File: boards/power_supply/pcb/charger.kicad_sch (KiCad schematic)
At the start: 42 parts, among them J301 Conn_01x02_Socket, J302 Conn_01x04_Socket

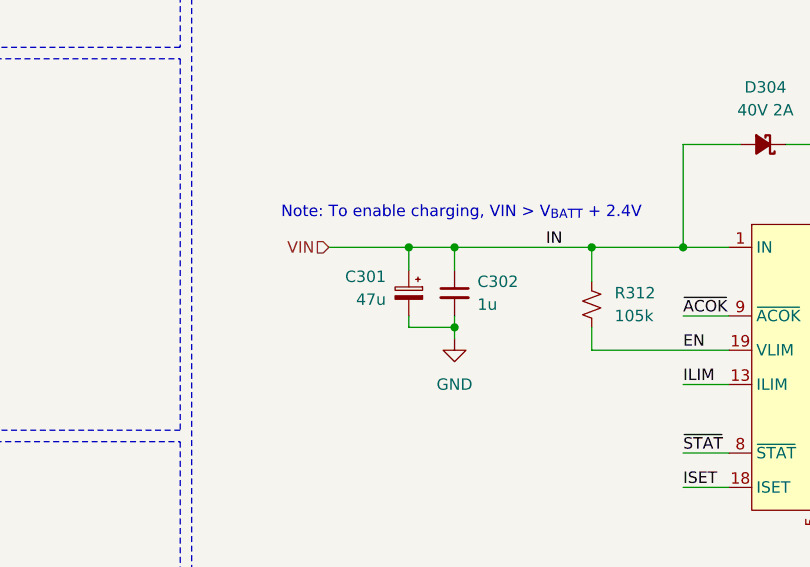
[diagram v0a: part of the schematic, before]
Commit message: psu schematic capture
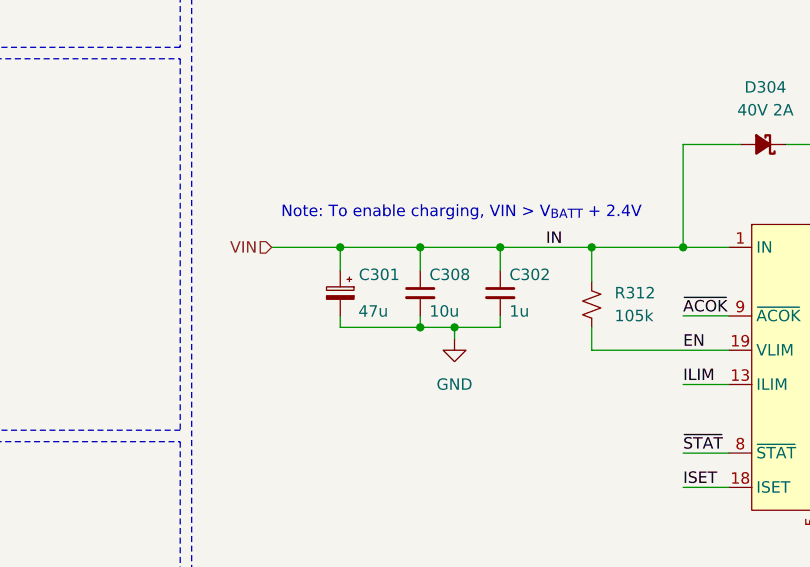
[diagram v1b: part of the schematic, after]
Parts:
- added C308: 10u, symbol Device:C_Small
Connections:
- net GND: now also C308.2
- net VIN: now also C308.1
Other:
- moved on the sheet: C301
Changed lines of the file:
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@@
 	)
 	(junction
-		(at 146.05 80.01)
+		(at 147.32 88.9)
 		(diameter 0)
 		(color 0 0 0 0)
@@
 	)
 	(junction
+		(at 147.32 80.01)
+		(diameter 0)
+		(color 0 0 0 0)
+	)
+	(junction
 		(at 240.03 99.06)
 		(diameter 0)
@@
 	)
 	(junction
-		(at 151.13 80.01)
+		(at 138.43 80.01)
 		(diameter 0)
 		(color 0 0 0 0)
@@
 	)
 	(junction
+		(at 156.21 80.01)
+		(diameter 0)
+		(color 0 0 0 0)
+	)
+	(junction
 		(at 198.12 113.03)
 		(diameter 0)
@@
 	(wire
 		(pts
-			(xy 151.13 80.01) (xy 151.13 82.55)
+			(xy 156.21 80.01) (xy 156.21 82.55)
 		)
 		(stroke
@@
 	(wire
 		(pts
-			(xy 146.05 80.01) (xy 151.13 80.01)
+			(xy 64.77 72.39) (xy 64.77 73.66)
 		)
 		(stroke
@@
 	(wire
 		(pts
-			(xy 64.77 72.39) (xy 64.77 73.66)
+			(xy 176.53 80.01) (xy 181.61 80.01)
 		)
 		(stroke
@@
 	(wire
 		(pts
-			(xy 176.53 80.01) (xy 181.61 80.01)
+			(xy 151.13 88.9) (xy 151.13 90.17)
 		)
 		(stroke
@@
 	(wire
 		(pts
-			(xy 151.13 88.9) (xy 151.13 90.17)
+			(xy 138.43 80.01) (xy 147.32 80.01)
 		)
 		(stroke
@@
 	(wire
 		(pts
-			(xy 151.13 80.01) (xy 166.37 80.01)
-		)
-		(stroke
-			(width 0)
-			(type default)
-		)
-	)
-	(wire
-		(pts
 			(xy 39.37 44.45) (xy 39.37 45.72)
 		)
@@
 	(wire
 		(pts
-			(xy 146.05 88.9) (xy 151.13 88.9)
+			(xy 138.43 88.9) (xy 147.32 88.9)
 		)
 		(stroke
@@
 	(wire
 		(pts
+			(xy 156.21 80.01) (xy 166.37 80.01)
+		)
+		(stroke
+			(width 0)
+			(type default)
+		)
+	)
+	(wire
+		(pts
 			(xy 64.77 44.45) (xy 64.77 45.72)
 		)
@@
 	(wire
 		(pts
-			(xy 137.16 80.01) (xy 146.05 80.01)
+			(xy 130.81 80.01) (xy 138.43 80.01)
 		)
 		(stroke
@@
 	(wire
 		(pts
+			(xy 147.32 80.01) (xy 147.32 82.55)
+		)
+		(stroke
+			(width 0)
+			(type default)
+		)
+	)
+	(wire
+		(pts
 			(xy 229.87 54.61) (xy 229.87 59.69)
 		)
@@
 	(wire
 		(pts
-			(xy 146.05 87.63) (xy 146.05 88.9)
+			(xy 138.43 87.63) (xy 138.43 88.9)
 		)
 		(stroke
@@
 	(wire
 		(pts
+			(xy 147.32 88.9) (xy 151.13 88.9)
+		)
+		(stroke
+			(width 0)
+			(type default)
+		)
+	)
+	(wire
+		(pts
 			(xy 207.01 76.2) (xy 210.82 76.2)
 		)
@@
 	(wire
 		(pts
-			(xy 146.05 80.01) (xy 146.05 82.55)
+			(xy 138.43 80.01) (xy 138.43 82.55)
+		)
+		(stroke
+			(width 0)
+			(type default)
+		)
+	)
+	(wire
+		(pts
+			(xy 147.32 87.63) (xy 147.32 88.9)
 		)
 		(stroke
@@
 	(wire
 		(pts
+			(xy 147.32 80.01) (xy 156.21 80.01)
+		)
+		(stroke
+			(width 0)
+			(type default)
+		)
+	)
+	(wire
+		(pts
 			(xy 50.8 161.29) (xy 50.8 162.56)
 		)
@@
 	(wire
 		(pts
+			(xy 156.21 88.9) (xy 151.13 88.9)
+		)
+		(stroke
+			(width 0)
+			(type default)
+		)
+	)
+	(wire
+		(pts
 			(xy 194.31 74.93) (xy 194.31 68.58)
 		)
@@
 	(wire
 		(pts
-			(xy 151.13 87.63) (xy 151.13 88.9)
+			(xy 156.21 87.63) (xy 156.21 88.9)
 		)
 		(stroke
@@
 	(hierarchical_label "VIN"
 		(shape input)
-		(at 137.16 80.01 180)
+		(at 130.81 80.01 180)
 		(fields_autoplaced yes)
 		(effects
@@
 	)
 	(symbol
-		(lib_id "Device:C_Small")
-		(at 151.13 85.09 0)
-		(unit 1)
-		(exclude_from_sim no)
-		(in_bom yes)
-		(on_board yes)
-		(dnp no)
-		(fields_autoplaced yes)
-		(property "Reference" "C302"
-			(at 153.67 83.8262 0)
-			(effects
-				(font
-					(size 1.27 1.27)
-				)
-				(justify left)
-			)
-		)
-		(property "Value" "1u"
-			(at 153.67 86.3662 0)
-			(effects
-				(font
-					(size 1.27 1.27)
-				)
-				(justify left)
-			)
-		)
-		(property "Footprint" ""
-			(at 151.13 85.09 0)
-			(effects
-				(font
-					(size 1.27 1.27)
-				)
-				(hide yes)
-			)
-		)
-		(property "Datasheet" "~"
-			(at 151.13 85.09 0)
-			(effects
-				(font
-					(size 1.27 1.27)
-				)
-				(hide yes)
-			)
-		)
-		(property "Description" "Unpolarized capacitor, small symbol"
-			(at 151.13 85.09 0)
-			(effects
-				(font
-					(size 1.27 1.27)
-				)
-				(hide yes)
-			)
-		)
-		(pin "1"
-		)
-		(pin "2"
-		)
-		(instances
-			(project "power_supply"
-				(path "/6a7d9dc9-f78f-470f-911b-b95256023173/00f00675-e615-4796-971e-104476714f1d"
-					(reference "C302")
-					(unit 1)
-				)
-			)
-		)
-	)
-	(symbol
 		(lib_id "power:GND")
 		(at 29.21 177.8 0)
@@
 	(symbol
 		(lib_id "Device:C_Polarized_Small")
-		(at 146.05 85.09 0)
+		(at 138.43 85.09 0)
 		(mirror y)
 		(unit 1)
@@
 		(dnp no)
 		(property "Reference" "C301"
-			(at 143.51 83.2738 0)
+			(at 145.034 83.058 0)
 			(effects
 				(font
@@
 		)
 		(property "Value" "47u"
-			(at 143.51 85.8138 0)
+			(at 143.764 87.122 0)
 			(effects
 				(font
@@
 		)
 		(property "Footprint" ""
-			(at 146.05 85.09 0)
+			(at 138.43 85.09 0)
 			(effects
 				(font
@@
 		)
 		(property "Datasheet" "~"
-			(at 146.05 85.09 0)
+			(at 138.43 85.09 0)
 			(effects
 				(font
@@
 		)
 		(property "Description" "Polarized capacitor, small symbol"
-			(at 146.05 85.09 0)
+			(at 138.43 85.09 0)
 			(effects
 				(font
@@
 	)
 	(symbol
+		(lib_id "Device:C_Small")
+		(at 147.32 85.09 0)
+		(unit 1)
+		(exclude_from_sim no)
+		(in_bom yes)
+		(on_board yes)
+		(dnp no)
+		(property "Reference" "C308"
+			(at 148.336 83.058 0)
+			(effects
+				(font
+					(size 1.27 1.27)
+				)
+				(justify left)
+			)
+		)
+		(property "Value" "10u"
+			(at 148.336 87.122 0)
+			(effects
+				(font
+					(size 1.27 1.27)
+				)
+				(justify left)
+			)
+		)
+		(property "Footprint" ""
+			(at 147.32 85.09 0)
+			(effects
+				(font
+					(size 1.27 1.27)
+				)
+				(hide yes)
+			)
+		)
+		(property "Datasheet" "~"
+			(at 147.32 85.09 0)
+			(effects
+				(font
+					(size 1.27 1.27)
+				)
+				(hide yes)
+			)
+		)
+		(property "Description" "Unpolarized capacitor, small symbol"
+			(at 147.32 85.09 0)
+			(effects
+				(font
+					(size 1.27 1.27)
+				)
+				(hide yes)
+			)
+		)
+		(pin "1"
+		)
+		(pin "2"
+		)
+		(instances
+			(project "power_supply"
+				(path "/6a7d9dc9-f78f-470f-911b-b95256023173/00f00675-e615-4796-971e-104476714f1d"
+					(reference "C308")
+					(unit 1)
+				)
+			)
+		)
+	)
+	(symbol
 		(lib_id "power:GND")
 		(at 39.37 134.62 0)
@@
 					(unit 1)
 				)
+			)
+		)
+	)
+	(symbol
+		(lib_id "Device:C_Small")
+		(at 156.21 85.09 0)
+		(unit 1)
+		(exclude_from_sim no)
+		(in_bom yes)
+		(on_board yes)
+		(dnp no)
+		(property "Reference" "C302"
+			(at 157.226 83.058 0)
+			(effects
+				(font
+					(size 1.27 1.27)
+				)
+				(justify left)
+			)
+		)
+		(property "Value" "1u"
+			(at 157.226 87.122 0)
+			(effects
+				(font
+					(size 1.27 1.27)
+				)
+				(justify left)
+			)
+		)
+		(property "Footprint" ""
+			(at 156.21 85.09 0)
+			(effects
+				(font
+					(size 1.27 1.27)
+				)
+				(hide yes)
+			)
+		)
+		(property "Datasheet" "~"
+			(at 156.21 85.09 0)
+			(effects
+				(font
+					(size 1.27 1.27)
+				)
+				(hide yes)
+			)
+		)
+		(property "Description" "Unpolarized capacitor, small symbol"
+			(at 156.21 85.09 0)
+			(effects
+				(font
+					(size 1.27 1.27)
+				)
+				(hide yes)
+			)
+		)
+		(pin "1"
+		)
+		(pin "2"
+		)
+		(instances
+			(project "power_supply"
+				(path "/6a7d9dc9-f78f-470f-911b-b95256023173/00f00675-e615-4796-971e-104476714f1d"
+					(reference "C302")
+					(unit 1)
+				)

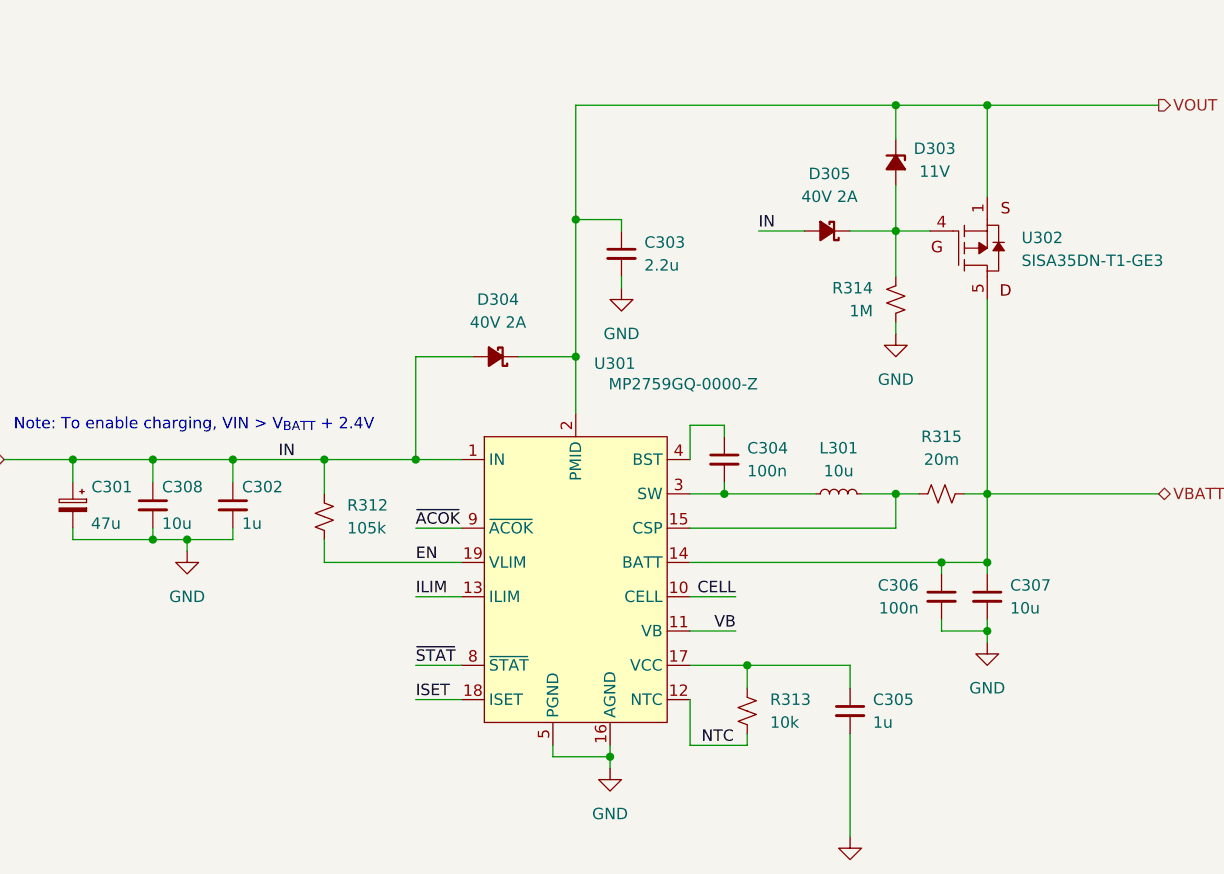
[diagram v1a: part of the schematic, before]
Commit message: psu schematic capture
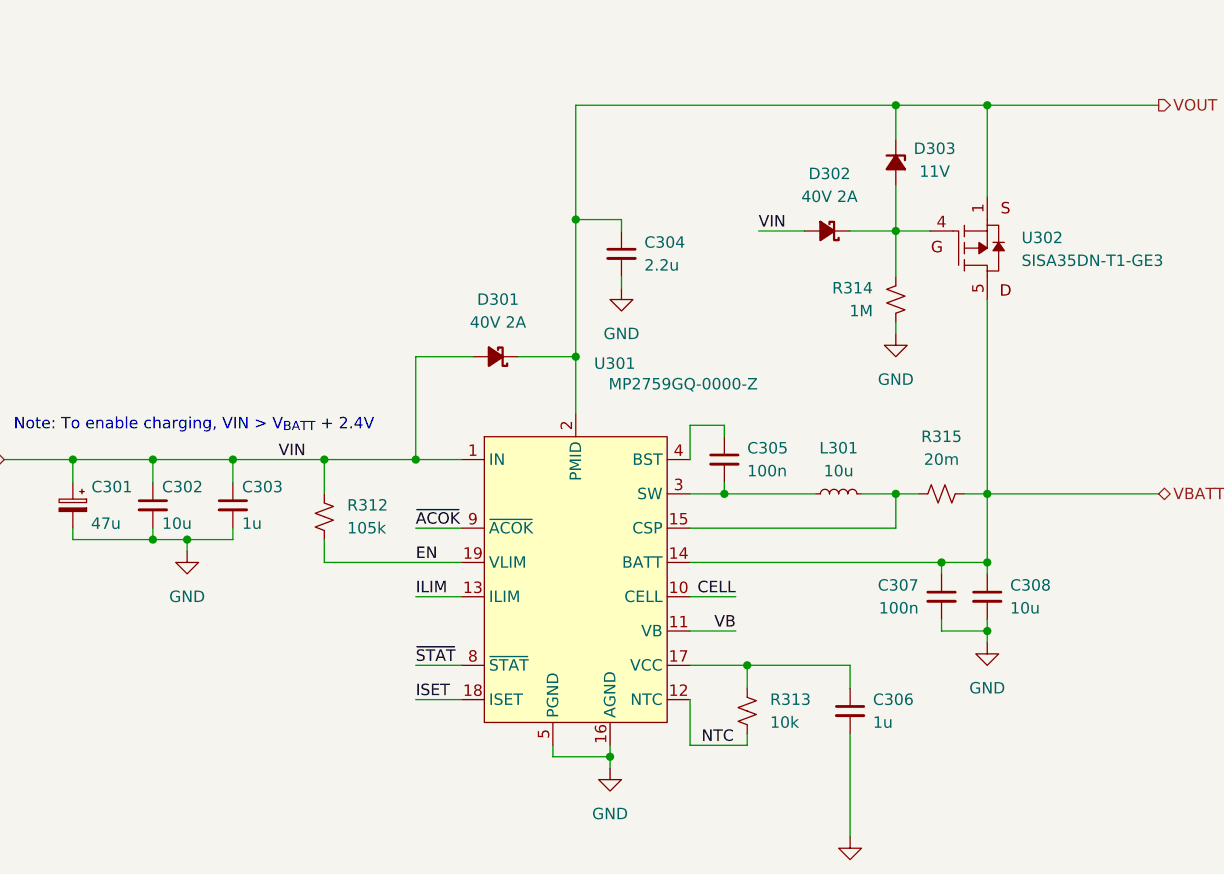
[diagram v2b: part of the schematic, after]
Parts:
- renumbered C308 to C302, C302 to C303, C303 to C304, C304 to C305, C305 to C306, C306 to C307, C307 to C308, D304 to D301, D305 to D302
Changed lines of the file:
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@@
 		)
 	)
-	(label "IN"
+	(label "VIN"
 		(at 161.29 80.01 0)
 		(fields_autoplaced yes)
@@
 		)
 	)
-	(label "IN"
+	(label "VIN"
 		(at 214.63 54.61 0)
 		(fields_autoplaced yes)
@@
 		(dnp no)
 		(fields_autoplaced yes)
-		(property "Reference" "D305"
+		(property "Reference" "D302"
 			(at 222.504 48.26 0)
 			(effects
@@
 			(project "power_supply"
 				(path "/6a7d9dc9-f78f-470f-911b-b95256023173/00f00675-e615-4796-971e-104476714f1d"
-					(reference "D305")
+					(reference "D302")
 					(unit 1)
 				)
@@
 		(on_board yes)
 		(dnp no)
-		(property "Reference" "C306"
+		(property "Reference" "C307"
 			(at 232.41 93.9862 0)
 			(effects
@@
 			(project "power_supply"
 				(path "/6a7d9dc9-f78f-470f-911b-b95256023173/00f00675-e615-4796-971e-104476714f1d"
-					(reference "C306")
+					(reference "C307")
 					(unit 1)
 				)
@@
 		(dnp no)
 		(fields_autoplaced yes)
-		(property "Reference" "C307"
+		(property "Reference" "C308"
 			(at 242.57 93.9862 0)
 			(effects
@@
 			(project "power_supply"
 				(path "/6a7d9dc9-f78f-470f-911b-b95256023173/00f00675-e615-4796-971e-104476714f1d"
-					(reference "C307")
+					(reference "C308")
 					(unit 1)
 				)
@@
 		(dnp no)
 		(fields_autoplaced yes)
-		(property "Reference" "C305"
+		(property "Reference" "C306"
 			(at 227.33 106.6862 0)
 			(effects
@@
 			(project ""
 				(path "/6a7d9dc9-f78f-470f-911b-b95256023173/00f00675-e615-4796-971e-104476714f1d"
-					(reference "C305")
+					(reference "C306")
 					(unit 1)
 				)
@@
 		(on_board yes)
 		(dnp no)
-		(property "Reference" "C308"
+		(property "Reference" "C302"
 			(at 148.336 83.058 0)
 			(effects
@@
 			(project "power_supply"
 				(path "/6a7d9dc9-f78f-470f-911b-b95256023173/00f00675-e615-4796-971e-104476714f1d"
-					(reference "C308")
+					(reference "C302")
 					(unit 1)
 				)
@@
 		(dnp no)
 		(fields_autoplaced yes)
-		(property "Reference" "C304"
+		(property "Reference" "C305"
 			(at 213.36 78.7462 0)
 			(effects
@@
 			(project "power_supply"
 				(path "/6a7d9dc9-f78f-470f-911b-b95256023173/00f00675-e615-4796-971e-104476714f1d"
-					(reference "C304")
+					(reference "C305")
 					(unit 1)
 				)
@@
 		(dnp no)
 		(fields_autoplaced yes)
-		(property "Reference" "C303"
+		(property "Reference" "C304"
 			(at 201.93 55.8862 0)
 			(effects
@@
 			(project "power_supply"
 				(path "/6a7d9dc9-f78f-470f-911b-b95256023173/00f00675-e615-4796-971e-104476714f1d"
-					(reference "C303")
+					(reference "C304")
 					(unit 1)
 				)
@@
 		(on_board yes)
 		(dnp no)
-		(property "Reference" "C302"
+		(property "Reference" "C303"
 			(at 157.226 83.058 0)
 			(effects
@@
 			(project "power_supply"
 				(path "/6a7d9dc9-f78f-470f-911b-b95256023173/00f00675-e615-4796-971e-104476714f1d"
-					(reference "C302")
+					(reference "C303")
 					(unit 1)
 				)
@@
 		(dnp no)
 		(fields_autoplaced yes)
-		(property "Reference" "D304"
+		(property "Reference" "D301"
 			(at 185.674 62.23 0)
 			(effects
@@
 			(project ""
 				(path "/6a7d9dc9-f78f-470f-911b-b95256023173/00f00675-e615-4796-971e-104476714f1d"
-					(reference "D304")
+					(reference "D301")
 					(unit 1)
 				)

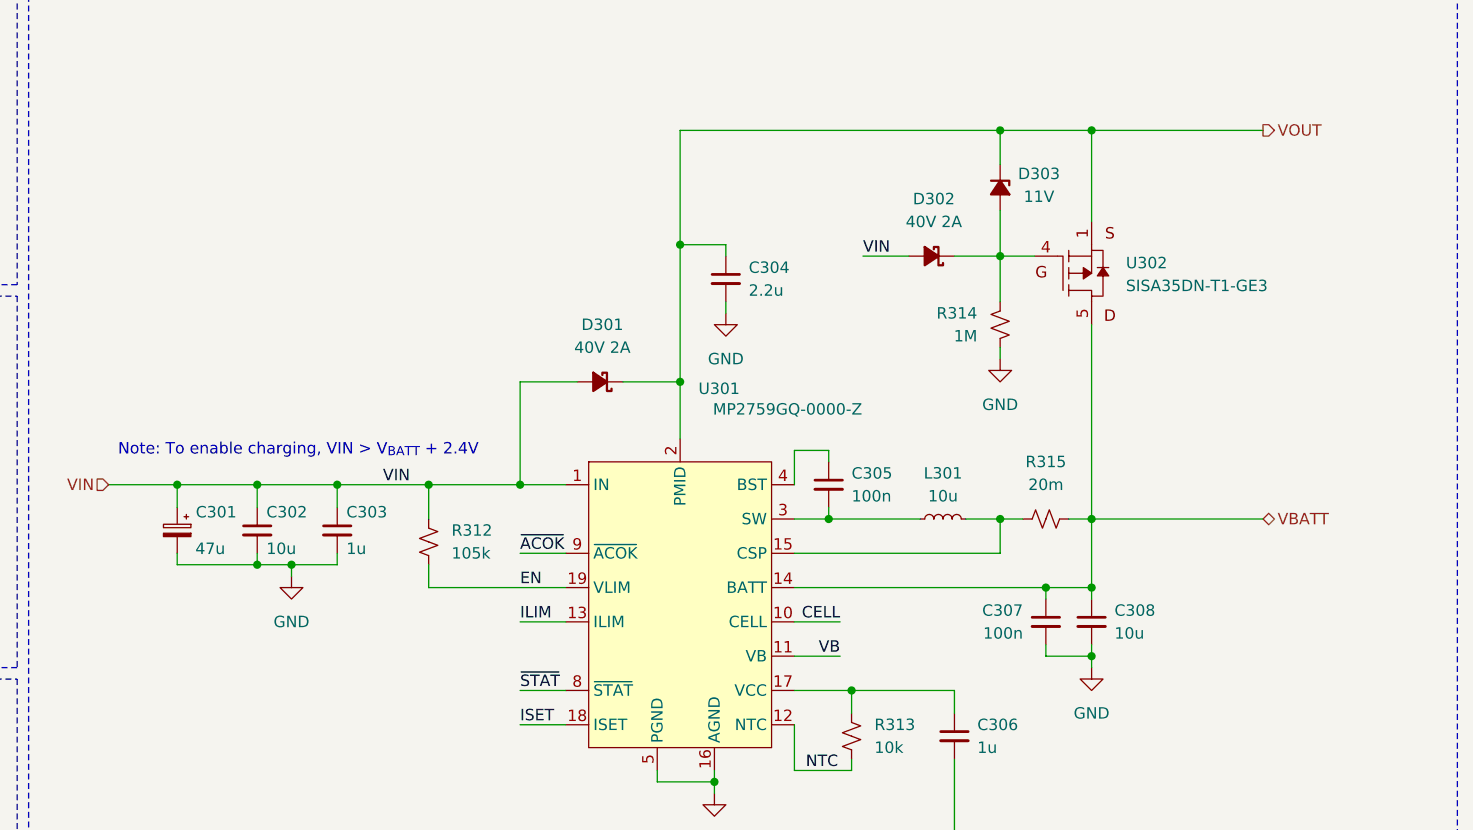
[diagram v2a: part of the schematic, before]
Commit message: psu component selection
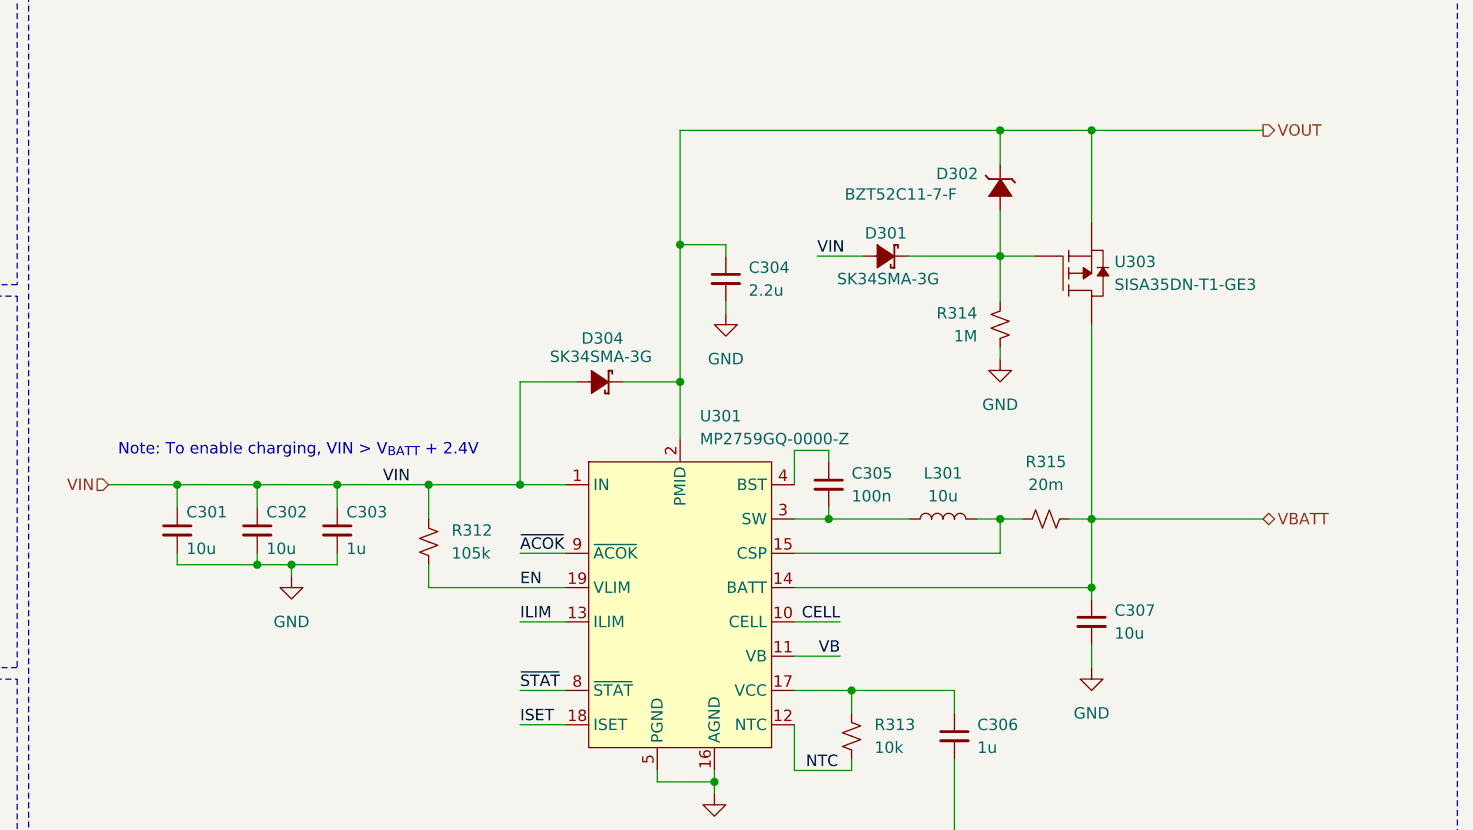
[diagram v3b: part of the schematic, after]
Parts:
- removed C301: 47u, symbol Device:C_Polarized_Small
- removed C307: 100n, symbol Device:C_Small
- removed D301, D302: 40V 2A, symbol Device:D_Schottky_Small_Filled
- removed D303: 11V, symbol Device:D_Zener_Small_Filled
- removed L301: 10u, symbol Device:L_Small
- removed U302: ~, symbol SISA35DN-T1-GE3:SISA35DN-T1-GE3
- added C301: 10u, symbol Device:C_Small
- added D301, D304: ~, symbol SK34SMA-3G:SK34SMA-3G
- added D302: ~, symbol BZT52C11-7-F:BZT52C11-7-F
- added L301: 10u, symbol Device:L
- added U303: ~, symbol SISA35DN-T1-GE3:SISA35DN-T1-GE3
- renumbered C308 to C307
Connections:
- net GND: now also C301.2
- net VBATT: now also U303.5, U303.6, U303.7, U303.8
- net VIN: now also C301.1, D301.2, D304.2
- net VOUT: now also D302.1, D304.1, U303.1, U303.2, U303.3
- net at C305.2, U301.3 (SW): now also L301.1
- net at R315.1, U301.15 (CSP): now also L301.2
- net at R314.1: now also D301.1, D302.2, U303.4
